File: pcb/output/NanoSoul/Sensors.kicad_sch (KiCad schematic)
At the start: 8 parts

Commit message: pcb: 3mm 白边 + J2/J7 离 J4 + DRC 丝印告警清零
- 最外围 3mm 白边：板放大到 94×92（Ø108 切边收小到 7/8mm），铜/器件焊盘距最外缘 ≥3mm
  （自动布线内缩 3mm；顶排 J5/J6 下移、J8 左移退出白边区）。
- J2/J7 离 J4：右月牙整体右移 1.6mm，离 J4 本体 +0.83mm（原相擦 0.78mm）。
- DRC = 0 warning：5 个位号(D4/D5/Q1/U1/U7)挪开、接线图例升到 0.8mm 并缩短、
  删 J3/J4 压挖孔丝印、隐藏 6 安装孔与 U7 位号。
- 17.8mm 母座行距核对通过；4 个 M3 安装孔成规则 54×82 矩形（旧版钉在 Ø108 圆外、钻不出，已修正）。
- 余 MOT_RTN/GND 各 1 段跨挖孔大电流网/地：按 docs 铁律出板前人工绕挖孔补（GND 建议铺地铜），
  网表连接关系正确（其余 170 网 0 短路）。原理图 ERC 不适用：circuit-synth 开源导出无导线、
  网表为真值源。详见 docs/05 §9.1。
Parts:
- C14, C15, C16, J8, R15, R16, U6, U7: hierarchy_path /8a83f0c7-8320-4874-8ea1-ef8ee28a330a/ae7345a0-e36a-47e4-a1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 -> /cc6d016d-315a-4023-b551-816edf85e992/fc4b519f-b46e-434e-9a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; root_uuid 8a83f0c7-8320-4874-8ea1-ef8ee28a330a -> cc6d016d-315a-4023-b551-816edf85e992
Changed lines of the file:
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@@
 			)
 		)
-		(property "hierarchy_path" "/8a83f0c7-8320-4874-8ea1-ef8ee28a330a/ae7345a0-e36a-47e4-a118-6b5d24bda4c7"
+		(property "hierarchy_path" "/cc6d016d-315a-4023-b551-816edf85e992/fc4b519f-b46e-434e-9a3f-274ec2644ccc"
 			(at 66.04 38.0999 0)
 			(effects
@@
 			)
 		)
-		(property "root_uuid" "8a83f0c7-8320-4874-8ea1-ef8ee28a330a"
+		(property "root_uuid" "cc6d016d-315a-4023-b551-816edf85e992"
 			(at 66.04 38.0999 0)
 			(effects
@@
 		(instances
 			(project ""
-				(path "/8a83f0c7-8320-4874-8ea1-ef8ee28a330a/ae7345a0-e36a-47e4-a118-6b5d24bda4c7"
+				(path "/cc6d016d-315a-4023-b551-816edf85e992/fc4b519f-b46e-434e-9a3f-274ec2644ccc"
 					(reference "U6")
 					(unit 1)
@@
 			)
 		)
-		(property "hierarchy_path" "/8a83f0c7-8320-4874-8ea1-ef8ee28a330a/ae7345a0-e36a-47e4-a118-6b5d24bda4c7"
+		(property "hierarchy_path" "/cc6d016d-315a-4023-b551-816edf85e992/fc4b519f-b46e-434e-9a3f-274ec2644ccc"
 			(at 226.06 38.0999 0)
 			(effects
@@
 			)
 		)
-		(property "root_uuid" "8a83f0c7-8320-4874-8ea1-ef8ee28a330a"
+		(property "root_uuid" "cc6d016d-315a-4023-b551-816edf85e992"
 			(at 226.06 38.0999 0)
 			(effects
@@
 		(instances
 			(project ""
-				(path "/8a83f0c7-8320-4874-8ea1-ef8ee28a330a/ae7345a0-e36a-47e4-a118-6b5d24bda4c7"
+				(path "/cc6d016d-315a-4023-b551-816edf85e992/fc4b519f-b46e-434e-9a3f-274ec2644ccc"
 					(reference "C14")
 					(unit 1)
@@
 			)
 		)
-		(property "hierarchy_path" "/8a83f0c7-8320-4874-8ea1-ef8ee28a330a/ae7345a0-e36a-47e4-a118-6b5d24bda4c7"
+		(property "hierarchy_path" "/cc6d016d-315a-4023-b551-816edf85e992/fc4b519f-b46e-434e-9a3f-274ec2644ccc"
 			(at 251.46 38.0999 0)
 			(effects
@@
 			)
 		)
-		(property "root_uuid" "8a83f0c7-8320-4874-8ea1-ef8ee28a330a"
+		(property "root_uuid" "cc6d016d-315a-4023-b551-816edf85e992"
 			(at 251.46 38.0999 0)
 			(effects
@@
 		(instances
 			(project ""
-				(path "/8a83f0c7-8320-4874-8ea1-ef8ee28a330a/ae7345a0-e36a-47e4-a118-6b5d24bda4c7"
+				(path "/cc6d016d-315a-4023-b551-816edf85e992/fc4b519f-b46e-434e-9a3f-274ec2644ccc"
 					(reference "C15")
 					(unit 1)
@@
 			)
 		)
-		(property "hierarchy_path" "/8a83f0c7-8320-4874-8ea1-ef8ee28a330a/ae7345a0-e36a-47e4-a118-6b5d24bda4c7"
+		(property "hierarchy_path" "/cc6d016d-315a-4023-b551-816edf85e992/fc4b519f-b46e-434e-9a3f-274ec2644ccc"
 			(at 139.7 35.5599 0)
 			(effects
@@
 			)
 		)
-		(property "root_uuid" "8a83f0c7-8320-4874-8ea1-ef8ee28a330a"
+		(property "root_uuid" "cc6d016d-315a-4023-b551-816edf85e992"
 			(at 139.7 35.5599 0)
 			(effects
@@
 		(instances
 			(project ""
-				(path "/8a83f0c7-8320-4874-8ea1-ef8ee28a330a/ae7345a0-e36a-47e4-a118-6b5d24bda4c7"
+				(path "/cc6d016d-315a-4023-b551-816edf85e992/fc4b519f-b46e-434e-9a3f-274ec2644ccc"
 					(reference "U7")
 					(unit 1)
@@
 			)
 		)
-		(property "hierarchy_path" "/8a83f0c7-8320-4874-8ea1-ef8ee28a330a/ae7345a0-e36a-47e4-a118-6b5d24bda4c7"
+		(property "hierarchy_path" "/cc6d016d-315a-4023-b551-816edf85e992/fc4b519f-b46e-434e-9a3f-274ec2644ccc"
 			(at 276.86 38.0999 0)
 			(effects
@@
 			)
 		)
-		(property "root_uuid" "8a83f0c7-8320-4874-8ea1-ef8ee28a330a"
+		(property "root_uuid" "cc6d016d-315a-4023-b551-816edf85e992"
 			(at 276.86 38.0999 0)
 			(effects
@@
 		(instances
 			(project ""
-				(path "/8a83f0c7-8320-4874-8ea1-ef8ee28a330a/ae7345a0-e36a-47e4-a118-6b5d24bda4c7"
+				(path "/cc6d016d-315a-4023-b551-816edf85e992/fc4b519f-b46e-434e-9a3f-274ec2644ccc"
 					(reference "C16")
 					(unit 1)
@@
 			)
 		)
-		(property "hierarchy_path" "/8a83f0c7-8320-4874-8ea1-ef8ee28a330a/ae7345a0-e36a-47e4-a118-6b5d24bda4c7"
+		(property "hierarchy_path" "/cc6d016d-315a-4023-b551-816edf85e992/fc4b519f-b46e-434e-9a3f-274ec2644ccc"
 			(at 177.8 40.6399 0)
 			(effects
@@
 			)
 		)
-		(property "root_uuid" "8a83f0c7-8320-4874-8ea1-ef8ee28a330a"
+		(property "root_uuid" "cc6d016d-315a-4023-b551-816edf85e992"
 			(at 177.8 40.6399 0)
 			(effects
@@
 		(instances
 			(project ""
-				(path "/8a83f0c7-8320-4874-8ea1-ef8ee28a330a/ae7345a0-e36a-47e4-a118-6b5d24bda4c7"
+				(path "/cc6d016d-315a-4023-b551-816edf85e992/fc4b519f-b46e-434e-9a3f-274ec2644ccc"
 					(reference "R15")
 					(unit 1)
@@
 			)
 		)
-		(property "hierarchy_path" "/8a83f0c7-8320-4874-8ea1-ef8ee28a330a/ae7345a0-e36a-47e4-a118-6b5d24bda4c7"
+		(property "hierarchy_path" "/cc6d016d-315a-4023-b551-816edf85e992/fc4b519f-b46e-434e-9a3f-274ec2644ccc"
 			(at 200.66 40.6399 0)
 			(effects
@@
 			)
 		)
-		(property "root_uuid" "8a83f0c7-8320-4874-8ea1-ef8ee28a330a"
+		(property "root_uuid" "cc6d016d-315a-4023-b551-816edf85e992"
 			(at 200.66 40.6399 0)
 			(effects
@@
 		(instances
 			(project ""
-				(path "/8a83f0c7-8320-4874-8ea1-ef8ee28a330a/ae7345a0-e36a-47e4-a118-6b5d24bda4c7"
+				(path "/cc6d016d-315a-4023-b551-816edf85e992/fc4b519f-b46e-434e-9a3f-274ec2644ccc"
 					(reference "R16")
 					(unit 1)
@@
 			)
 		)
-		(property "hierarchy_path" "/8a83f0c7-8320-4874-8ea1-ef8ee28a330a/ae7345a0-e36a-47e4-a118-6b5d24bda4c7"
+		(property "hierarchy_path" "/cc6d016d-315a-4023-b551-816edf85e992/fc4b519f-b46e-434e-9a3f-274ec2644ccc"
 			(at 33.02 93.9799 0)
 			(effects
@@
 			)
 		)
-		(property "root_uuid" "8a83f0c7-8320-4874-8ea1-ef8ee28a330a"
+		(property "root_uuid" "cc6d016d-315a-4023-b551-816edf85e992"
 			(at 33.02 93.9799 0)
 			(effects
@@
 		(instances
 			(project ""
-				(path "/8a83f0c7-8320-4874-8ea1-ef8ee28a330a/ae7345a0-e36a-47e4-a118-6b5d24bda4c7"
+				(path "/cc6d016d-315a-4023-b551-816edf85e992/fc4b519f-b46e-434e-9a3f-274ec2644ccc"
 					(reference "J8")
 					(unit 1)

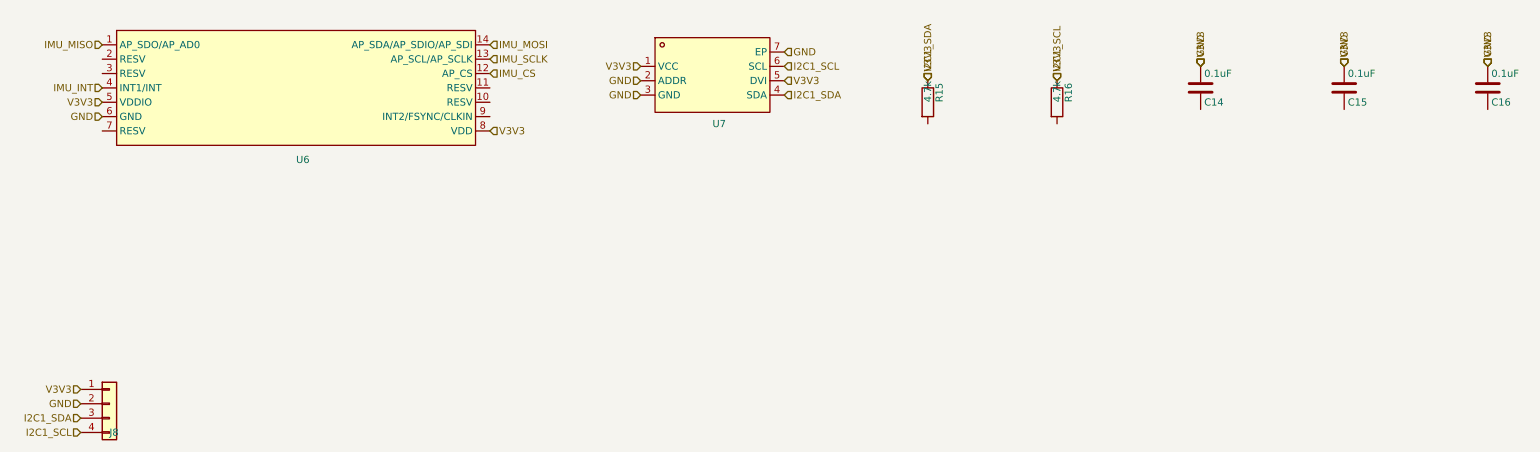
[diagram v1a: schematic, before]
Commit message: pcb: schematic-parity 真零(零 ignore) + 重导 Gerber
DRC `--schematic-parity --severity-all` = 0 violation / 0 unconnected /
0 schematic-parity,62 项检查全置 error、零 ignore(旧版的 7 项 ignore 全部真修掉,
非关检查)。verify_board 65/65、布线 778 走线+60 过孔未动。

- 修通 circuit-synth 原理图连通性:它把一器件所有网名标签堆在 pin1 → KiCad 推断错网。
  按 .net 逐脚在真实连接点重放 global_label(fix_sch_labels),net_conflict 199→0;
  真 NC 脚在板上配同名 unconnected- 网对齐(assign_nc_nets)。
- 板 Value 回填真实值(顺修「板上 Value=封装名」的 BOM bug)、lib_id 去库前缀(fix_board_meta);
  原理图删 circuit-synth 私有字段/封装过滤器、补缺失 Value(fix_sch_fields);
  J2 attr→through_hole(USB-C 靠屏蔽脚 THT 安装,属实);4×M3 孔标 board_only。
- 唯一保留例外 = J2(USB-C)连接器内部 DRU(实测 0.10mm 铜/0.185mm 孔,JLC 可造;
  KiCad 官方 USB_C_Receptacle_HRO 封装内部孔距也仅 0.15mm → 换封装消不掉、
  改窄焊盘会伤实焊。限 J2 内部两两对象,不放宽对板上走线)。
- 重导 Gerber(9 层 Protel 扩展名 + Excellon 钻孔)+ BOM/CPL。
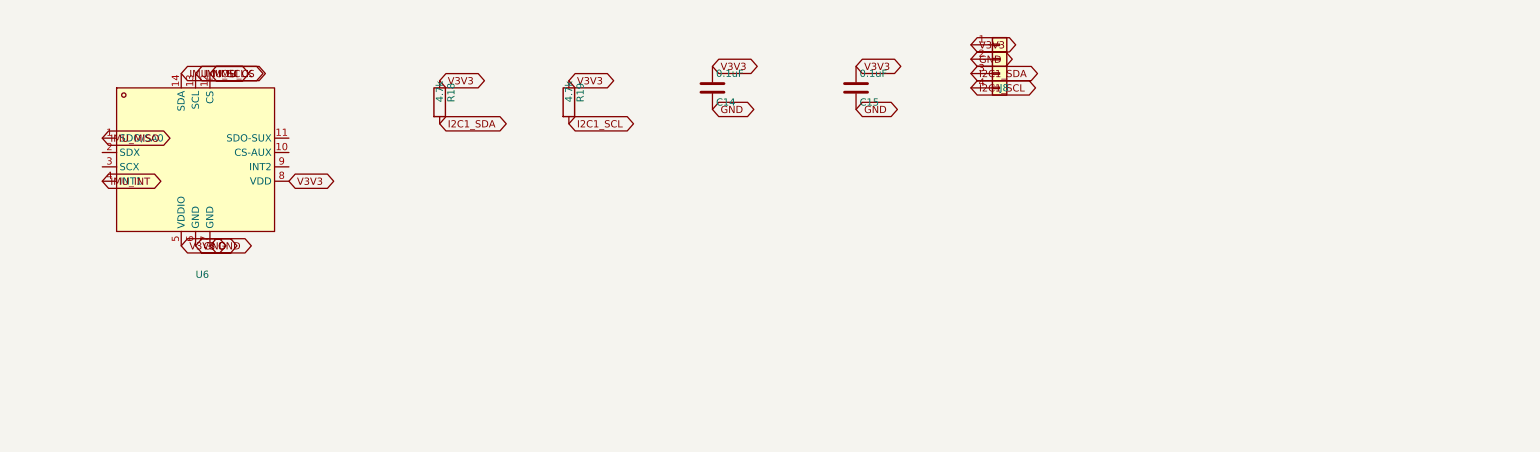
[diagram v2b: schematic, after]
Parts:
- removed C16: 0.1uF, Capacitor_SMD:C_0603_1608Metric, symbol Device:C
- removed R15, R16: 4.7k, Resistor_SMD:R_0603_1608Metric, symbol Device:R
- removed U6: (no value), nanosoul:LGA-14_L3.0-W2.5-P0.50-TL, symbol nanosoul:ICM-42688-P
- removed U7: (no value), nanosoul:WSOF-6_L2.6-W1.6-P0.50-TL-EP, symbol nanosoul:BH1750FVI-TR
- added R18, R19: 4.7k, R_0603_1608Metric, symbol Device:R
- added U6: LGA-14_L3.0-W2.5-P0.50-BR, LGA-14_L3.0-W2.5-P0.50-BR, symbol nanosoul:QMI8658C
- C14, C15: footprint Capacitor_SMD:C_0603_1608Metric -> C_0603_1608Metric; hierarchy_path /cc6d016d-315a-4023-b551-816edf85e992/fc4b519f-b46e-434e-9a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 -> (none); project_name NanoSoul -> (none); root_uuid cc6d016d-315a-4023-b551-816edf85e992 -> (none)
- J8: value (none) -> JST_SH_BM04B-SRSS-TB_1x04-1MP_P1.00mm_Vertical; footprint Connector_JST:JST_SH_BM04B-SRSS-TB_1x04-1MP_P1.00mm_Vertical -> JST_SH_BM04B-SRSS-TB_1x04-1MP_P1.00mm_Vertical; hierarchy_path /cc6d016d-315a-4023-b551-816edf85e992/fc4b519f-b46e-434e-9a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 -> (none); project_name NanoSoul -> (none); root_uuid cc6d016d-315a-4023-b551-816edf85e992 -> (none)
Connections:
- net GND: now also C14.2, C15.2, U6.6 (GND), U6.7 (GND); no longer C14.1, C15.1, J8.1 (Pin_1), J8.3 (Pin_3), J8.4 (Pin_4)
- net IMU_CS: now also U6.12 (CS)
- net IMU_INT: now also U6.4 (INT1)
- net IMU_MISO: now also U6.1 (SDO/SA0)
- net IMU_MOSI: now also U6.14 (SDA)
- net IMU_SCLK: now also U6.13 (SCL)
- new net I2C1_SCL: J8.4 (Pin_4), R19.2
- new net I2C1_SDA: J8.3 (Pin_3), R18.2
- new net V3V3: C14.1, C15.1, J8.1 (Pin_1), R18.1, R19.1, U6.5 (VDDIO), U6.8 (VDD)
